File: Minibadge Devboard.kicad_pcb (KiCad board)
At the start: 2 copper layers, 30.5 x 48.3 mm, 45 parts, among them J1 External power, J2 External switch, SW1 Power, SW3 SPEED, SW4 NTC

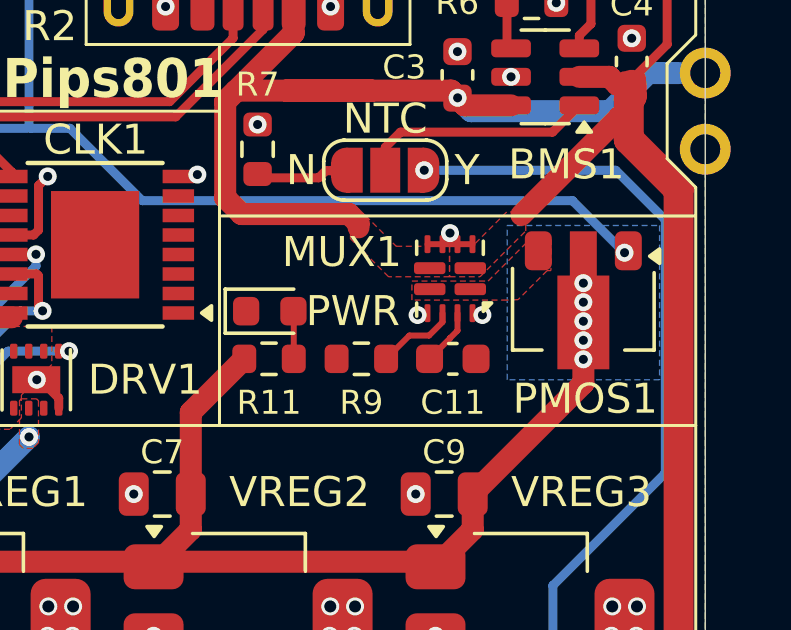
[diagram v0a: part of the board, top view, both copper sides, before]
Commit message: Add 3d model for TPS2121
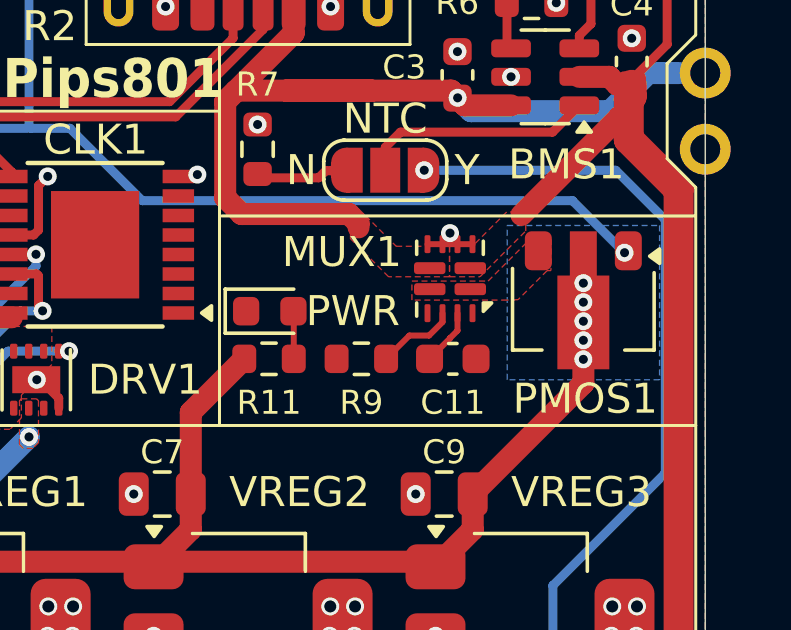
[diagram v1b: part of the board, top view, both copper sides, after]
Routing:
- net GND: vias 49 -> 47
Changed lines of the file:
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@@
 			)
 		)
+		(model "${KIPRJMOD}/Components/TPS2121/RUX0012A.stp"
+			(offset
+				(xyz 0 0 0)
+			)
+			(scale
+				(xyz 1 1 1)
+			)
+			(rotate
+				(xyz 0 0 0)
+			)
+		)
 	)
 	(footprint "SK12D07VG3-T:SW-SMD_SK12D07VG3-T"
@@
 	)
 	(via
-		(at 188.1505 110.617)
-		(size 0.6)
-		(drill 0.3)
-		(layers "F.Cu" "B.Cu")
-		(free yes)
-		(net 19)
-	)
-	(via
 		(at 183.09 100.335)
 		(size 0.6)
@@
 		(net 19)
 	)
-	(via
-		(at 185.9915 110.617)
-		(size 0.6)
-		(drill 0.3)
-		(layers "F.Cu" "B.Cu")
-		(free yes)
-		(net 19)
-	)
 	(segment
 		(start 171.080356 106.614356)
@@
 		(hatch edge 0.5)
 		(connect_pads yes
-			(clearance 0.4)
+			(clearance 0.3)
 		)
-		(min_thickness 0.3)
+		(min_thickness 0.25)
 		(filled_areas_thickness no)
 		(fill yes

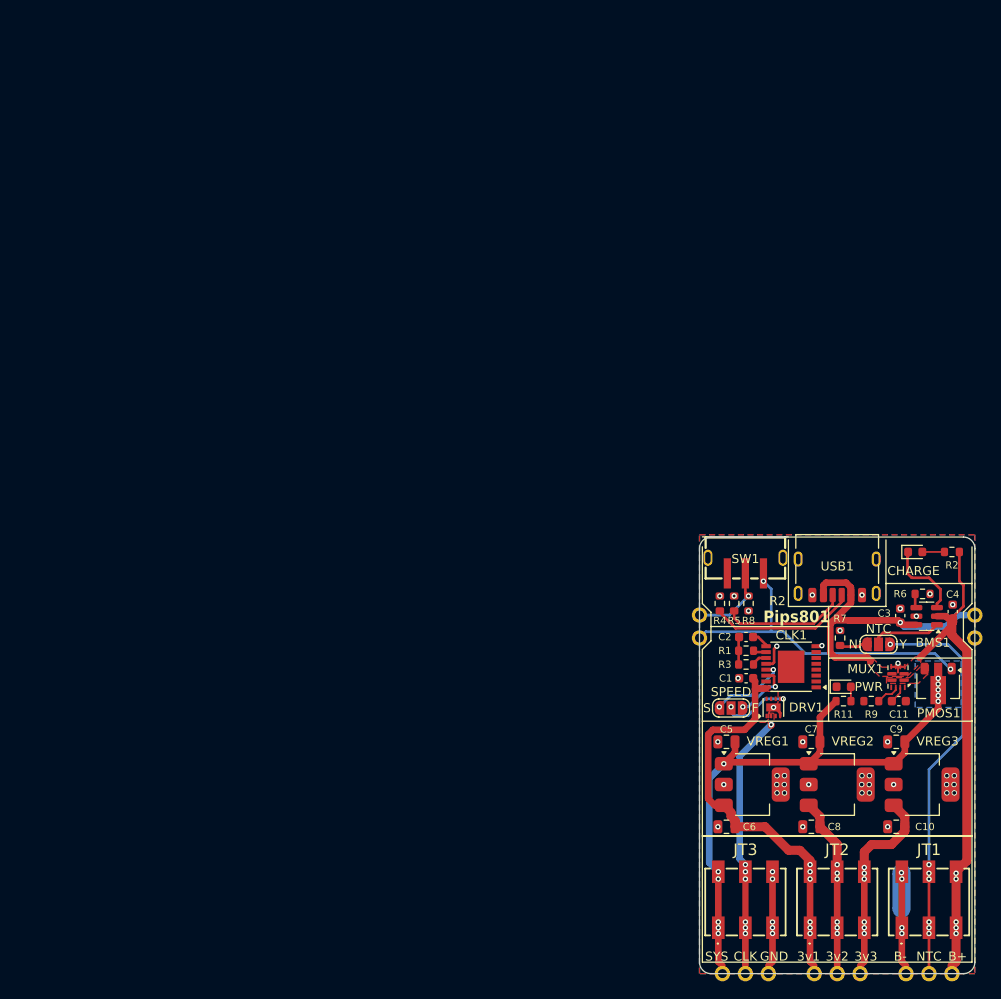
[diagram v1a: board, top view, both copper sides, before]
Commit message: Add 3d model for switch
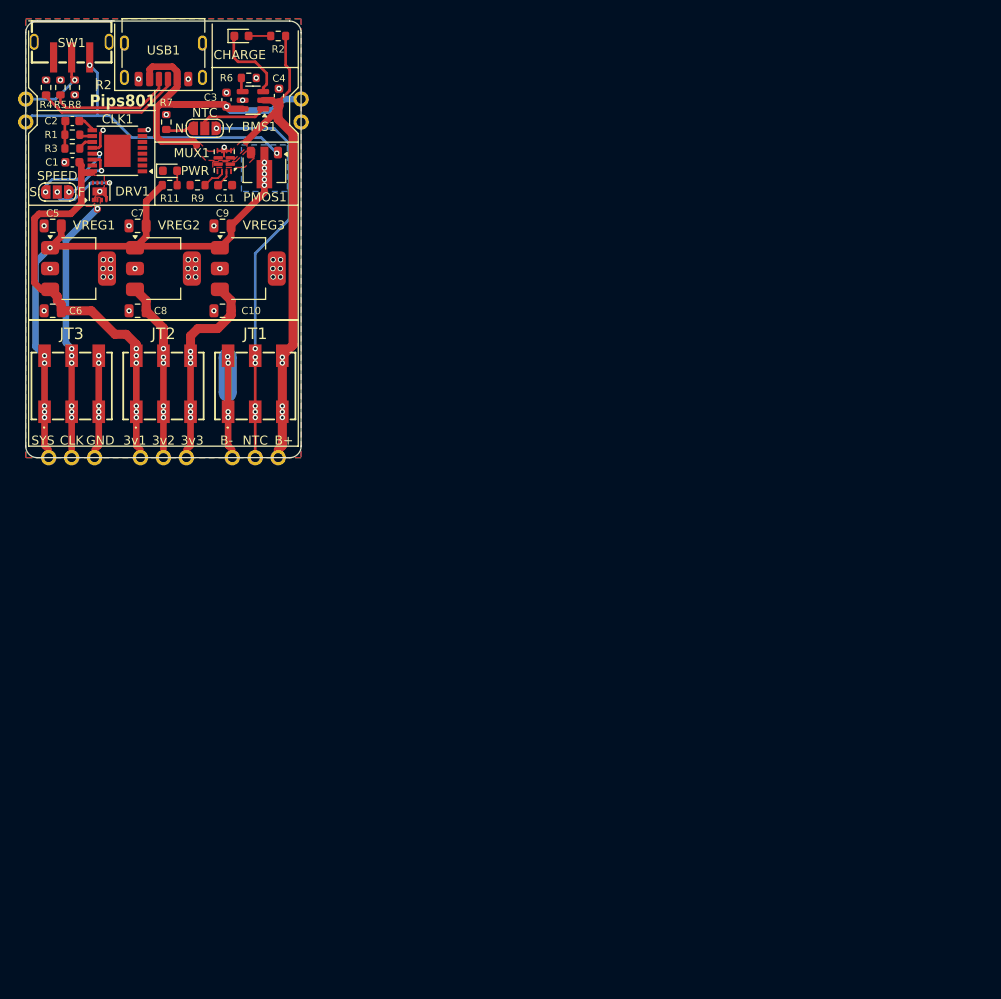
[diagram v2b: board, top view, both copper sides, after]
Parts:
- moved CLK1 93.9 mm to (100.7, 51.2)
- moved JC3 93.9 mm to (95.6, 85.1)
- moved JT3 93.9 mm to (95.6, 77.2)
- moved VREG1 93.9 mm to (96.4, 64.2)
- moved BMS1 93.9 mm to (115.7, 45.6)
- moved C1 93.9 mm to (95.7, 52.4)
- moved C11 93.9 mm to (112.6, 55.0)
- moved C2 93.9 mm to (95.7, 47.9)
- moved C4 93.9 mm to (118.6, 45.1)
- moved C5 93.9 mm to (93.5, 59.5)
- moved DRV1 93.9 mm to (98.7, 55.7)
- moved G*** 93.9 mm to (104.2, 59.7)
- moved J1 93.9 mm to (121.0, 48.0)
- moved J2 93.9 mm to (90.5, 48.0)
- moved JC1 93.9 mm to (115.9, 85.1)
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
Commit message: update traces
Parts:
- moved SW3 0.15 mm to (94.2, 55.7)
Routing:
- net NTC: track 46.1 -> 45.4 mm
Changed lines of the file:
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@@
 	(footprint "Jumper:SolderJumper-3_P1.3mm_Open_RoundedPad1.0x1.5mm_NumberLabels"
 		(layer "F.Cu")
-		(at 94.0185 55.728)
+		(at 94.1705 55.728)
 		(descr "SMD Solder 3-pad Jumper, 1x1.5mm rounded Pads, 0.3mm gap, open, labeled with numbers")
 		(tags "solder jumper open")
@@
 	)
 	(segment
-		(start 115.926 62.5225)
-		(end 119.6725 58.776)
+		(start 115.926 73.0635)
+		(end 115.926 62.5225)
 		(width 0.3)
 		(layer "B.Cu")
@@
 	)
 	(segment
-		(start 118.0215 48.6795)
-		(end 111.638 48.6795)
+		(start 115.926 73.0635)
+		(end 115.926 74.651)
 		(width 0.3)
 		(layer "B.Cu")
@@
 	)
 	(segment
-		(start 115.926 73.0635)
-		(end 115.926 62.5225)
+		(start 115.926 62.5225)
+		(end 119.6725 58.776)
 		(width 0.3)
 		(layer "B.Cu")
@@
 	)
 	(segment
-		(start 115.926 73.0635)
-		(end 115.926 74.651)
+		(start 116.8785 48.6795)
+		(end 111.638 48.6795)
 		(width 0.3)
 		(layer "B.Cu")
@@
 	(segment
 		(start 119.6725 58.776)
-		(end 119.6725 50.3305)
+		(end 119.6725 51.4735)
 		(width 0.3)
 		(layer "B.Cu")
@@
 	)
 	(segment
-		(start 119.6725 50.3305)
-		(end 118.0215 48.6795)
+		(start 119.6725 51.4735)
+		(end 116.8785 48.6795)
 		(width 0.3)
 		(layer "B.Cu")
@@
 	)
 	(via
-		(at 94.0185 55.728)
+		(at 94.1705 55.728)
 		(size 0.6)
 		(drill 0.3)
@@
 	)
 	(segment
-		(start 97.765 54.712)
-		(end 95.9235 56.5535)
-		(width 0.3)
-		(layer "B.Cu")
-		(net 17)
-	)
-	(segment
 		(start 95.9235 56.5535)
-		(end 94.336 56.5535)
+		(end 94.996 56.5535)
 		(width 0.3)
 		(layer "B.Cu")
@@
 	)
 	(segment
-		(start 94.0185 56.236)
-		(end 94.0185 55.728)
+		(start 97.765 54.712)
+		(end 95.9235 56.5535)
 		(width 0.3)
 		(layer "B.Cu")
@@
 	)
 	(segment
-		(start 94.336 56.5535)
-		(end 94.0185 56.236)
+		(start 94.996 56.5535)
+		(end 94.1705 55.728)
 		(width 0.3)
 		(layer "B.Cu")
@@
 	)
 	(via
-		(at 92.7185 55.728)
+		(at 92.8705 55.728)
 		(size 0.6)
 		(drill 0.3)
@@
 	)
 	(segment
-		(start 93.447 54.331)
+		(start 93.6875 54.331)
 		(end 96.241 54.331)
 		(width 0.3)
@@
 	)
 	(segment
-		(start 98.696999 51.875001)
-		(end 98.696999 51.483559)
+		(start 92.8705 55.728)
+		(end 92.8705 55.148)
 		(width 0.3)
 		(layer "B.Cu")
@@
 	)
 	(segment
-		(start 92.7185 55.728)
-		(end 92.7185 55.0595)
+		(start 92.8705 55.148)
+		(end 93.6875 54.331)
 		(width 0.3)
 		(layer "B.Cu")
@@
 	)
 	(segment
-		(start 92.7185 55.0595)
-		(end 93.447 54.331)
+		(start 98.696999 51.875001)
+		(end 98.696999 51.483559)
 		(width 0.3)
 		(layer "B.Cu")
@@
 	)
 	(via
-		(at 95.3185 55.728)
+		(at 95.4705 55.728)
 		(size 0.6)
 		(drill 0.3)
@@
 	)
 	(segment
-		(start 98.156753 53.367747)
-		(end 98.917002 53.367747)
+		(start 95.4705 55.728)
+		(end 95.7965 55.728)
 		(width 0.3)
 		(layer "B.Cu")
@@
 	)
 	(segment
-		(start 95.7965 55.728)
-		(end 98.156753 53.367747)
+		(start 98.156753 53.367747)
+		(end 98.917002 53.367747)
 		(width 0.3)
 		(layer "B.Cu")
@@
 	)
 	(segment
-		(start 95.3185 55.728)
-		(end 95.7965 55.728)
+		(start 95.7965 55.728)
+		(end 98.156753 53.367747)
 		(width 0.3)
 		(layer "B.Cu")
